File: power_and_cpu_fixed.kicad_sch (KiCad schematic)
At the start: 242 parts, among them J1 CPU1 USB, J10 AUX GPIO 1, J11 CAN2 PLUG, J12 Conn_01x06, J13 ADC AUX 2, J14 AUX GPIO 2, J15 AUX Encoder, J17 CAN Output, J2 CAN Input, J21 Power Input, J3 Encoder 1, J4 Encoder 2, J5 Conn_01x06, J6 CPU2 USB, J7 Conn_01x02, J9 ADC AUX 1, Q7 Q_NMOS_GSD, SW1 SW_MEC_5G, SW2 SW_MEC_5G, SW3 CONFIG SWITCH, U10 SN74LVC1G07QDCKTQ1, U11 TLV1117LV33DCYR, U12 W25Q128JVSIQ, U13 W25Q128JVSIQ, U15 RP2040, U16 ADC081S021CISD/NOPB, U17 isolator, U18 MCP2515-xSO, U19 RP2040, U23 SN74LVC1G07QDCKTQ1, U24 MT2492, U25 NCP1117-5_SOT223, U26 ADC081S021CISD/NOPB, U27 USBLC6-2P6, U28 USBLC6-2P6, U29 USBLC6-4SC6, U30 USBLC6-4SC6, U31 USBLC6-4SC6, U32 TLV1117LV33DCYR, U33 TX4139, U34 LTV-208, U6 SN74LVC1G07QDCKTQ1, U9 ADC081S021CISD/NOPB, Y1 12MHz, Y2 12MHz, Y3 16MHz

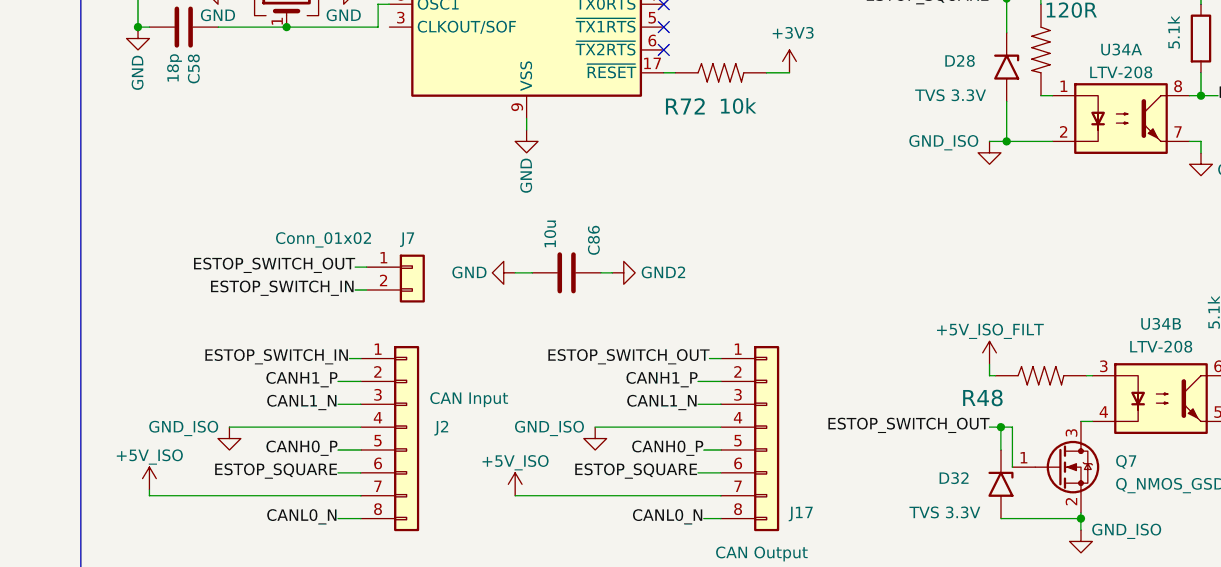
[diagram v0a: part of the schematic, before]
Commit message: Replaced global labels with normal net labels
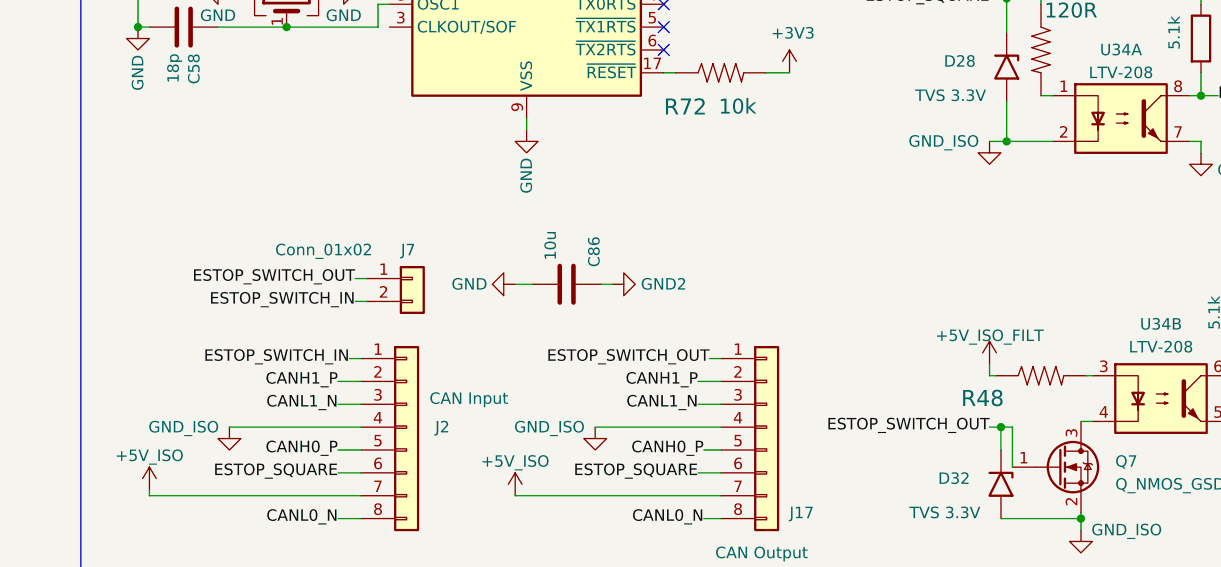
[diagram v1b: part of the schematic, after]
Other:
- moved on the sheet: C86, J7
